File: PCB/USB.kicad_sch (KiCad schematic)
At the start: 9 parts, among them J1 USB In, U1 TPD4E05U06, U5 TUSB321

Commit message: 17/08/2023 update
Moved gasket mounts from plate to PCB. Changed USB C connector. Modified case to accommodate. Tweaked thumb scroll holder.
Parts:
- J1: footprint Honeydew:HRO-TYPE-C-31-M-13x -> Honeydew:USB_C_Receptacle_G-Switch_GT-USB-7010ASV; LCSC C3019720 -> C165948
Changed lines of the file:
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@@
       (effects (font (size 1.27 1.27)))
     )
-    (property "Footprint" "Honeydew:HRO-TYPE-C-31-M-13x" (at 36.83 45.72 0)
+    (property "Footprint" "Honeydew:USB_C_Receptacle_G-Switch_GT-USB-7010ASV" (at 36.83 45.72 0)
       (effects (font (size 1.27 1.27)) hide)
     )
@@
       (effects (font (size 1.27 1.27)) hide)
     )
-    (property "LCSC" "C3019720" (at 33.02 45.72 0)
+    (property "LCSC" "C165948" (at 33.02 45.72 0)
       (effects (font (size 1.27 1.27)) hide)
     )

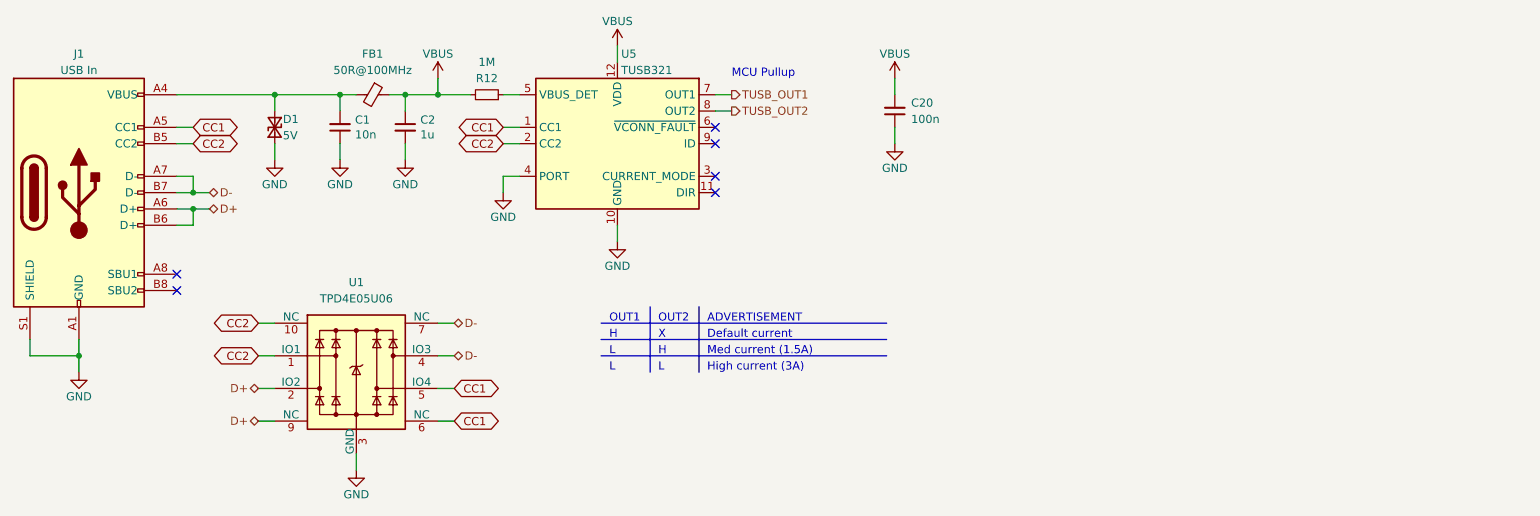
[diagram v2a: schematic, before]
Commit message: 27/08/2023 update
Added unified library for all symbols, footprints and 3D files. Changed MCU to STM32F072RBT6. Removed OLED, voltage and current sensing, USB CC circuitry and shift registers. Changed ESD protection chip. Cleaned up routing and component placement. Changed SWD header pinout to 6-pin standard.
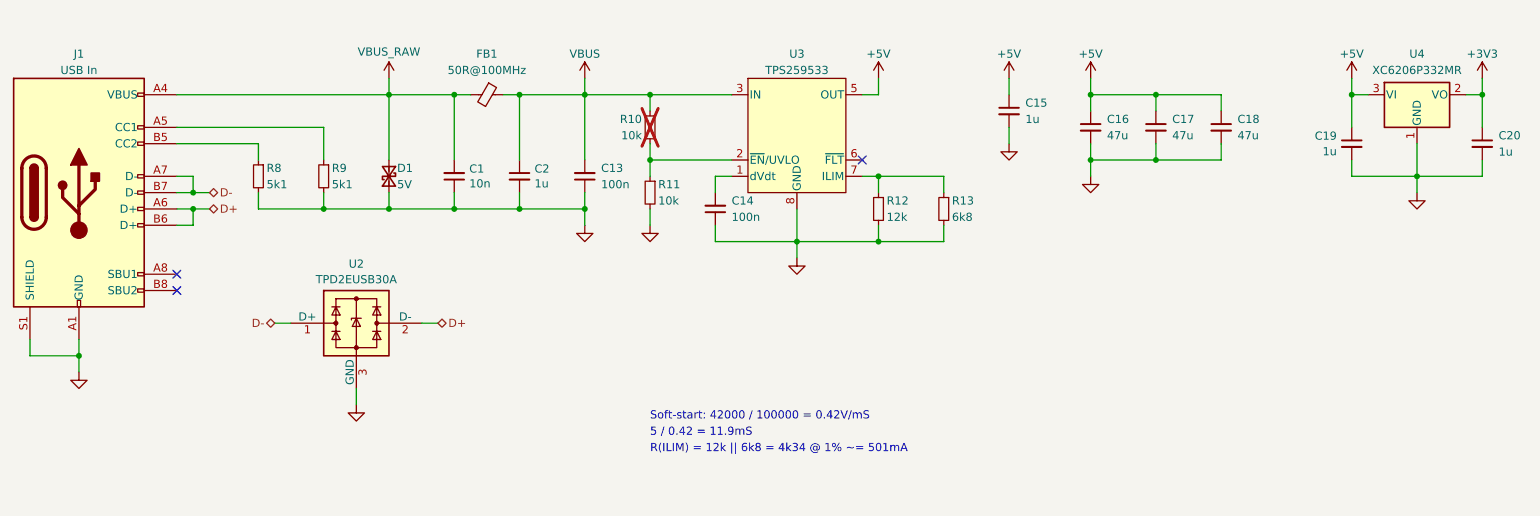
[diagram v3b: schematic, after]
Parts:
- removed U1: TPD4E05U06, Honeydew:USON-10_2.5x1.0mm_P0.5mm, symbol Galia:TPD4E05U06
- removed U5: TUSB321, Honeydew:Texas_X2QFN-12_1.6x1.6mm_P0.4mm, symbol Interface_USB:TUSB321
- added C13, C14: 100n, Ariamelon-Device:C_0402_1005Metric, symbol Device:C_Small
- added C15, C19: 1u, Ariamelon-Device:C_0402_1005Metric, symbol Device:C_Small
- added C16, C17, C18: 47u, Ariamelon-Device:C_1206_3216Metric, symbol Device:C_Small
- added R10, R11: 10k, Ariamelon-Device:R_0402_1005Metric, symbol Device:R_Small
- added R13: 6k8, Ariamelon-Device:R_0402_1005Metric, symbol Device:R_Small
- added R8, R9: 5k1, Ariamelon-Device:R_0402_1005Metric, symbol Device:R_Small
- added U2: TPD2EUSB30A, Package_TO_SOT_SMD:Texas_DRT-3, symbol Power_Protection:TPD2EUSB30A
- added U3: TPS259533, Ariamelon-Package:WSON-8-1EP_2x2mm_P0.5mm_EP0.9x1.6mm, symbol Ariamelon-IC:TPS259533
- added U4: XC6206P332MR, Ariamelon-Package:SOT-23-3, symbol Regulator_Linear:XC6206PxxxMR
- C1: footprint Capacitor_SMD:C_0402_1005Metric -> Ariamelon-Device:C_0402_1005Metric
- C2: footprint Capacitor_SMD:C_0603_1608Metric -> Ariamelon-Device:C_0603_1608Metric
- C20: value 100n -> 1u; footprint Capacitor_SMD:C_0402_1005Metric -> Ariamelon-Device:C_0402_1005Metric; LCSC C307331 -> C52923; Voltage 50V -> 25V
- D1: symbol Galia:D_TVS_Small -> Ariamelon-Device:D_TVS_Small
- FB1: footprint Inductor_SMD:L_1206_3216Metric -> Ariamelon-Device:L_0805_2012Metric; LCSC C527600 -> C237300
- J1: footprint Honeydew:USB_C_Receptacle_G-Switch_GT-USB-7010ASV -> Ariamelon-Connector:G-Switch_GT-USB-7010ASV
- R12: value 1M -> 12k; footprint Resistor_SMD:R_0402_1005Metric -> Ariamelon-Device:R_0402_1005Metric; LCSC C26083 -> C25752
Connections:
- net D+: now also U2.2 (D-)
- net D-: now also U2.1 (D+)
- net GND: now also C20.2, R12.2, C13.1, C14.1, C15.2, C16.2, C17.2, C18.2, C19.2, R11.2, R13.2, R8.2, R9.2, U2.3 (GND), U3.8 (GND), U3.9 (GND), U4.1 (GND); no longer C20.1
- net VBUS: now also C13.2, R10.2, U3.3 (IN), U3.4 (IN); no longer C20.2, R12.2
- net VBUS_RAW: now reaches C1.2, D1.1 (K), FB1.2, J1.A4 (VBUS), J1.A9 (VBUS), J1.B4 (VBUS), J1.B9 (VBUS)
- net at R12.1: now also R13.1, U3.7 (ILIM)
- net CC1: no longer names the net of J1.A5 (CC1)
- net CC1: now also R9.1
- net CC2: no longer names the net of J1.B5 (CC2)
- net CC2: now also R8.1
- new net: C14.2, U3.1 (dVdt)
- new net: R10.1, R11.1, U3.2 (~{EN}/UVLO)
- new net +3V3: C20.1, U4.2 (VO)
- new net +5V: C15.1, C16.1, C17.1, C18.1, C19.1, U3.5 (OUT), U4.3 (VI)
- no-connect marks 6 -> 3
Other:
- note added: "5 / 0.42 = 11.9mS"
- note added: "R(ILIM) = 12k || 6k8 = 4k34 @ 1% ~= 501mA"
- note added: "Soft-start: 42000 / 100000 = 0.42V/mS"
- note removed: "ADVERTISEMENT"
- note removed: "Default current"
- note removed: "H"
- note removed: "High current (3A)"
- note removed: "L"
- note removed: "MCU Pullup"
- note removed: "Med current (1.5A)"
- note removed: "OUT1"
- note removed: "OUT2"
- note removed: "X"
- moved on the sheet: C1, C2, FB1

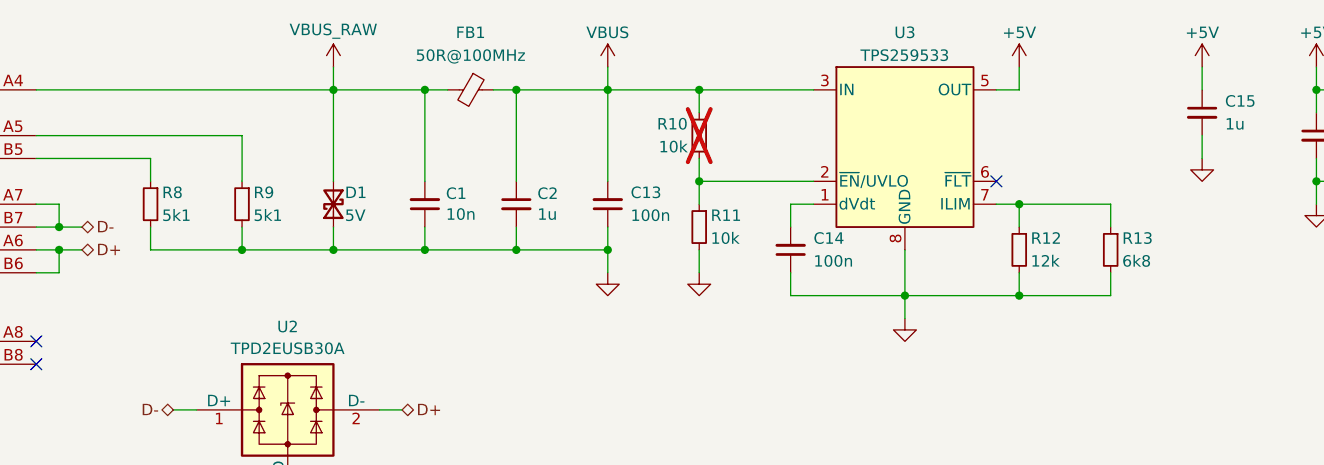
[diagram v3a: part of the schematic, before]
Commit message: 28/08/2023 update
Added test points for VIK connector. Refined case and scrollwheel design. Added pull-up resistor to RGB trace. Added Acheron single-push reset circuit. Updated STEP files.
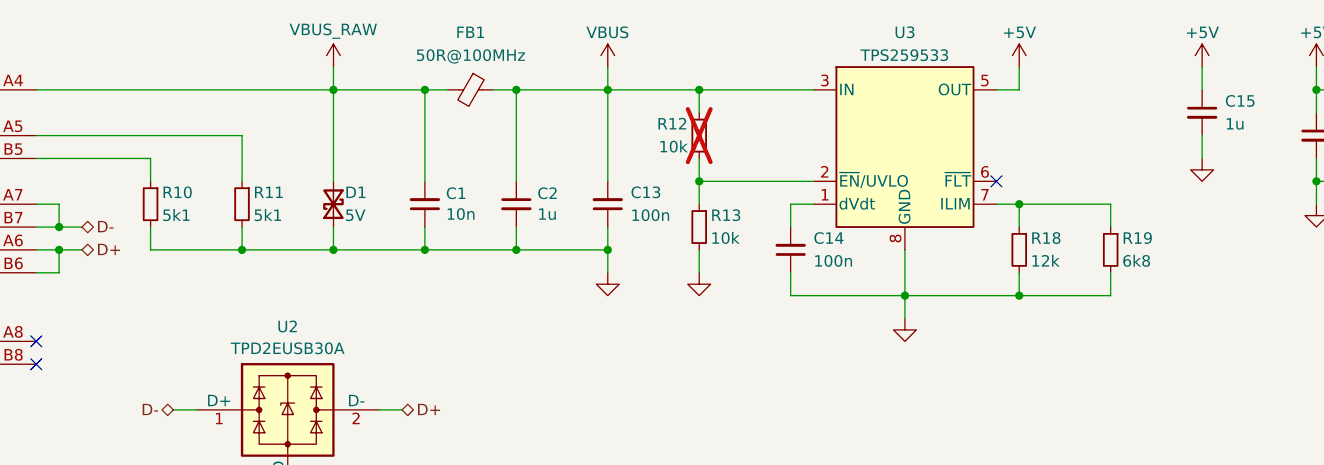
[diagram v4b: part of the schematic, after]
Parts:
- renumbered R8 to R10, R9 to R11, R10 to R12, R11 to R13, R12 to R18, R13 to R19
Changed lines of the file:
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@@
   (title_block
     (title "Honeydew unified split ergonomic keyboard")
-    (date "2023-08-27")
+    (date "2023-08-28")
     (rev "V3.0")
     (company "Created by Ariamelon (https://github.com/Ariamelon/Honeydew/)")
@@
   (symbol (lib_id "Device:R_Small") (at 60.96 43.18 0) (mirror y) (unit 1)
     (in_bom yes) (on_board yes) (dnp no)
-    (property "Reference" "R8" (at 62.23 41.91 0)
+    (property "Reference" "R10" (at 62.23 41.91 0)
       (effects (font (size 1.27 1.27)) (justify right))
     )
@@
       (project "Honeydew"
         (path "/534caec7-cf60-4f90-b1ed-42c9d445ef0f/03fe79d8-f43d-4879-be7c-5a505456d728"
-          (reference "R8") (unit 1)
+          (reference "R10") (unit 1)
         )
       )
@@
   (symbol (lib_id "Device:R_Small") (at 121.92 35.56 0) (mirror x) (unit 1)
     (in_bom no) (on_board yes) (dnp yes)
-    (property "Reference" "R10" (at 120.65 34.29 0)
+    (property "Reference" "R12" (at 120.65 34.29 0)
       (effects (font (size 1.27 1.27)) (justify right))
     )
@@
       (project "Honeydew"
         (path "/534caec7-cf60-4f90-b1ed-42c9d445ef0f/03fe79d8-f43d-4879-be7c-5a505456d728"
-          (reference "R10") (unit 1)
+          (reference "R12") (unit 1)
         )
       )
@@
   (symbol (lib_id "Device:R_Small") (at 71.12 43.18 0) (mirror y) (unit 1)
     (in_bom yes) (on_board yes) (dnp no)
-    (property "Reference" "R9" (at 72.39 41.91 0)
+    (property "Reference" "R11" (at 72.39 41.91 0)
       (effects (font (size 1.27 1.27)) (justify right))
     )
@@
       (project "Honeydew"
         (path "/534caec7-cf60-4f90-b1ed-42c9d445ef0f/03fe79d8-f43d-4879-be7c-5a505456d728"
-          (reference "R9") (unit 1)
+          (reference "R11") (unit 1)
         )
       )
@@
         )
         (path "/534caec7-cf60-4f90-b1ed-42c9d445ef0f/03fe79d8-f43d-4879-be7c-5a505456d728"
-          (reference "C10") (unit 1)
+          (reference "C11") (unit 1)
         )
       )
@@
   (symbol (lib_id "Device:R_Small") (at 167.64 48.26 0) (mirror y) (unit 1)
     (in_bom yes) (on_board yes) (dnp no)
-    (property "Reference" "R13" (at 168.91 46.99 0)
+    (property "Reference" "R19" (at 168.91 46.99 0)
       (effects (font (size 1.27 1.27)) (justify right))
     )
@@
       (project "Honeydew"
         (path "/534caec7-cf60-4f90-b1ed-42c9d445ef0f/03fe79d8-f43d-4879-be7c-5a505456d728"
-          (reference "R13") (unit 1)
+          (reference "R19") (unit 1)
         )
       )
@@
   (symbol (lib_id "Device:R_Small") (at 121.92 45.72 0) (mirror y) (unit 1)
     (in_bom yes) (on_board yes) (dnp no)
-    (property "Reference" "R11" (at 123.19 44.45 0)
+    (property "Reference" "R13" (at 123.19 44.45 0)
       (effects (font (size 1.27 1.27)) (justify right))
     )
@@
       (project "Honeydew"
         (path "/534caec7-cf60-4f90-b1ed-42c9d445ef0f/03fe79d8-f43d-4879-be7c-5a505456d728"
-          (reference "R11") (unit 1)
+          (reference "R13") (unit 1)
         )
       )
@@
       (effects (font (size 1.27 1.27)) hide)
     )
-    (property "Description" "50R@100MHz" (at 96.52 30.48 0)
+    (property "Description" "60R@100MHz" (at 96.52 30.48 0)
       (effects (font (size 1.27 1.27)) hide)
     )
@@
   (symbol (lib_id "Device:R_Small") (at 157.48 48.26 0) (mirror y) (unit 1)
     (in_bom yes) (on_board yes) (dnp no)
-    (property "Reference" "R12" (at 158.75 46.99 0)
+    (property "Reference" "R18" (at 158.75 46.99 0)
       (effects (font (size 1.27 1.27)) (justify right))
     )
@@
       (project "Honeydew"
         (path "/534caec7-cf60-4f90-b1ed-42c9d445ef0f/03fe79d8-f43d-4879-be7c-5a505456d728"
-          (reference "R12") (unit 1)
-        )
-      )
+          (reference "R18") (unit 1)
+        )
+      )

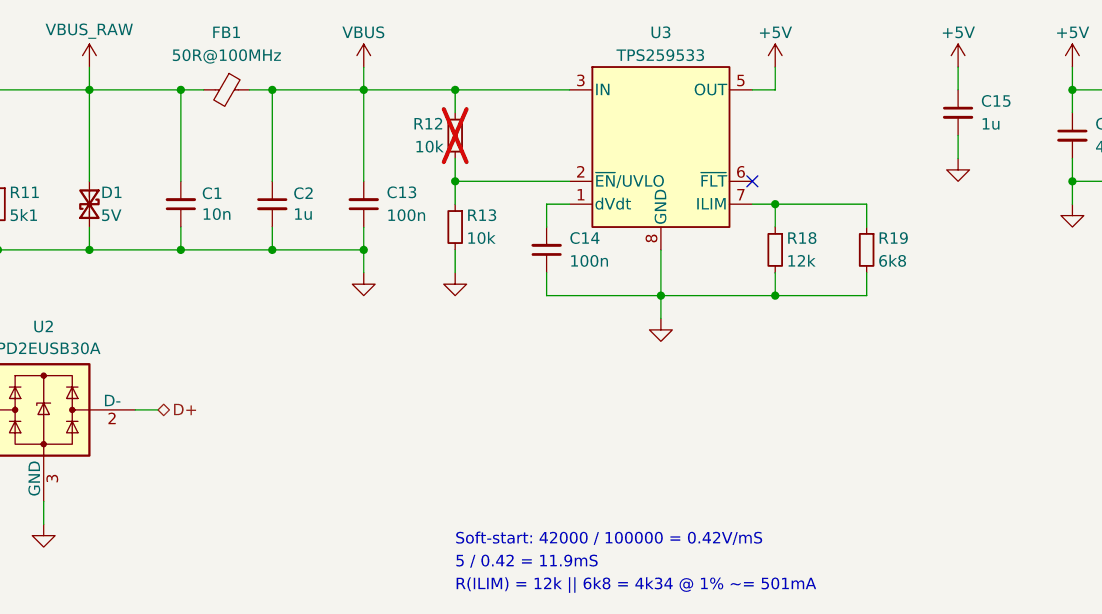
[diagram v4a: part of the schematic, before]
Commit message: 29/08/2023 update
Reassigned I2C pins due to DMA issues and rerouted board. Added test point for BOOT0. Added additional ground vias.
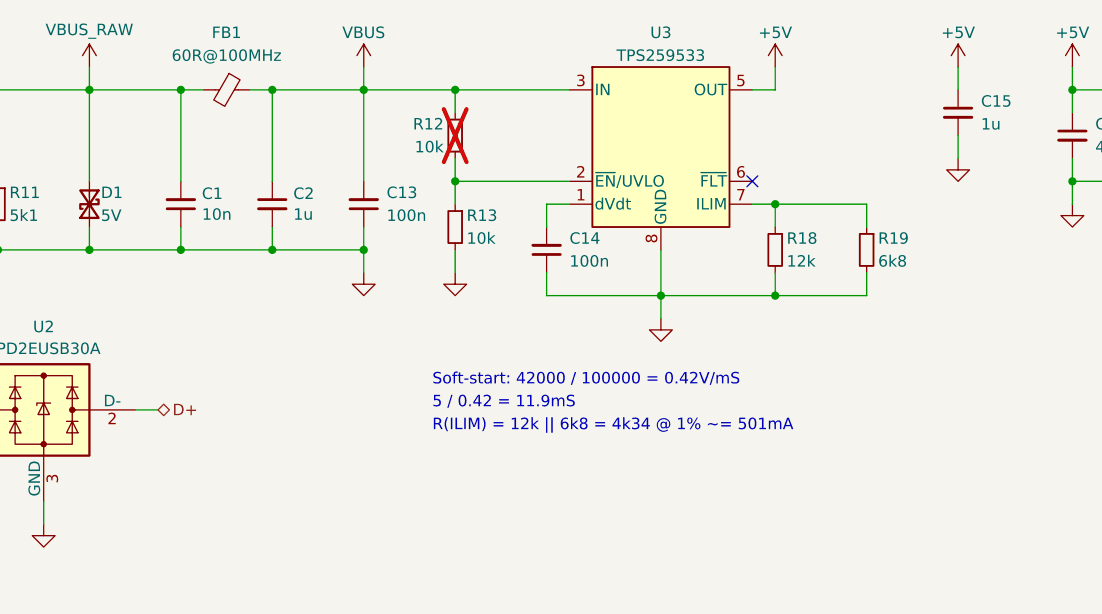
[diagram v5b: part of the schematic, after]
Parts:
- FB1: value 50R@100MHz -> 60R@100MHz
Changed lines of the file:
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@@
   (title_block
     (title "Honeydew unified split ergonomic keyboard")
-    (date "2023-08-28")
+    (date "2023-08-29")
     (rev "V3.0")
     (company "Created by Ariamelon (https://github.com/Ariamelon/Honeydew/)")
@@
     (stroke (width 0) (type default))
   )
-  (text "Soft-start: 42000 / 100000 = 0.42V/mS" (at 121.92 81.28 0)
+  (text "Soft-start: 42000 / 100000 = 0.42V/mS" (at 119.38 63.5 0)
     (effects (font (size 1.27 1.27)) (justify left bottom))
   )
-  (text "5 / 0.42 = 11.9mS" (at 121.92 83.82 0)
+  (text "5 / 0.42 = 11.9mS" (at 119.38 66.04 0)
     (effects (font (size 1.27 1.27)) (justify left bottom))
   )
-  (text "R(ILIM) = 12k || 6k8 = 4k34 @ 1% ~= 501mA" (at 121.92 86.36 0)
+  (text "R(ILIM) = 12k || 6k8 = 4k34 @ 1% ~= 501mA" (at 119.38 68.58 0)
     (effects (font (size 1.27 1.27)) (justify left bottom))
   )
@@
       (effects (font (size 1.27 1.27)))
     )
-    (property "Value" "50R@100MHz" (at 96.52 26.67 90)
+    (property "Value" "60R@100MHz" (at 96.52 26.67 90)
       (effects (font (size 1.27 1.27)))
     )
